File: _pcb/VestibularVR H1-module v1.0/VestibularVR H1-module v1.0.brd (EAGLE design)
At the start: 55.9 x 56.9 mm, 73 parts, among them IC1 FT232RL, IC2 74LVC1G07DBV, IC3 TLV70033DDCR, IC4 74LVC1G07DBV, IC5 74LVC1G07DBV, IC6 74LVC1G07DBV, IC7 USBLC6-2SC6, IC8 ATXMEGA32A4U, J5 Optical_flow_1, J6 Optical_flow_2, X1 TSW-105-02-S-D, X7 22-23-2051

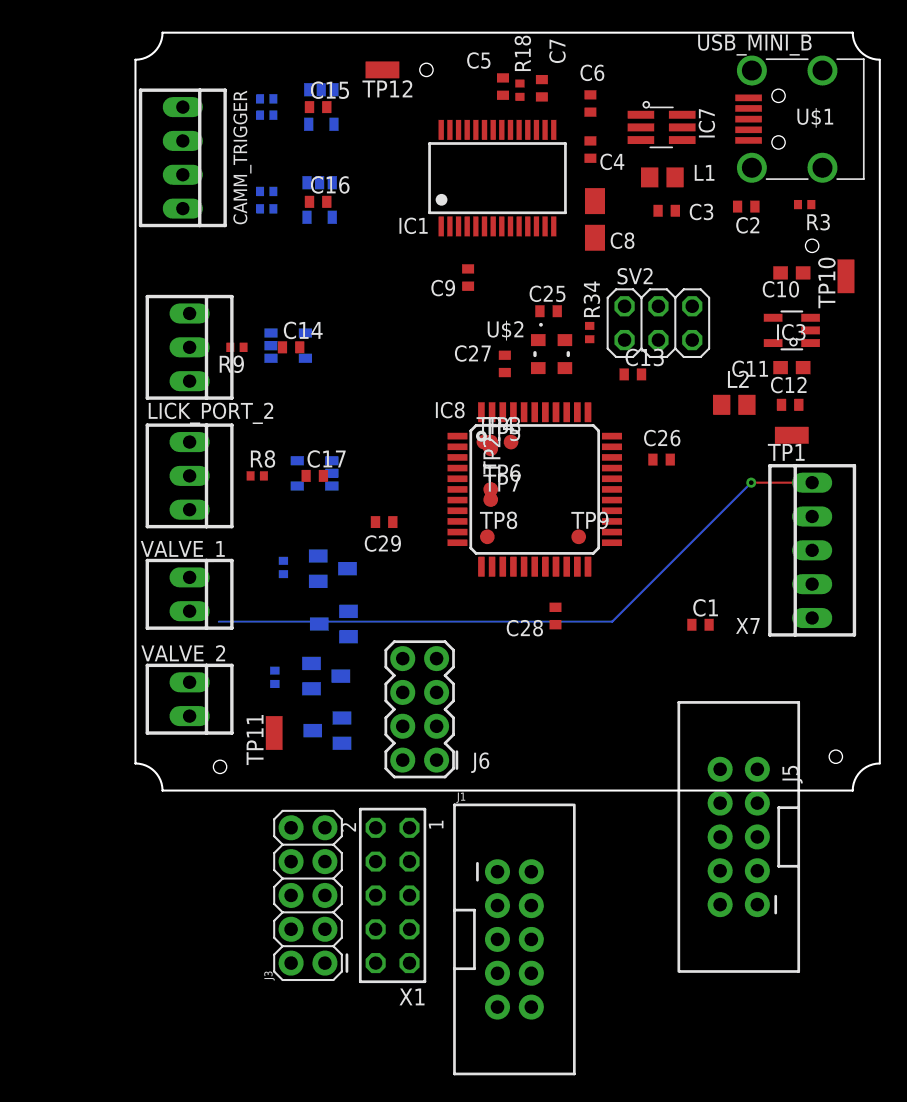
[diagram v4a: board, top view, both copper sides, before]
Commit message: . schm design reviewed 2nd time with Filipe . pcb design already started; not finished
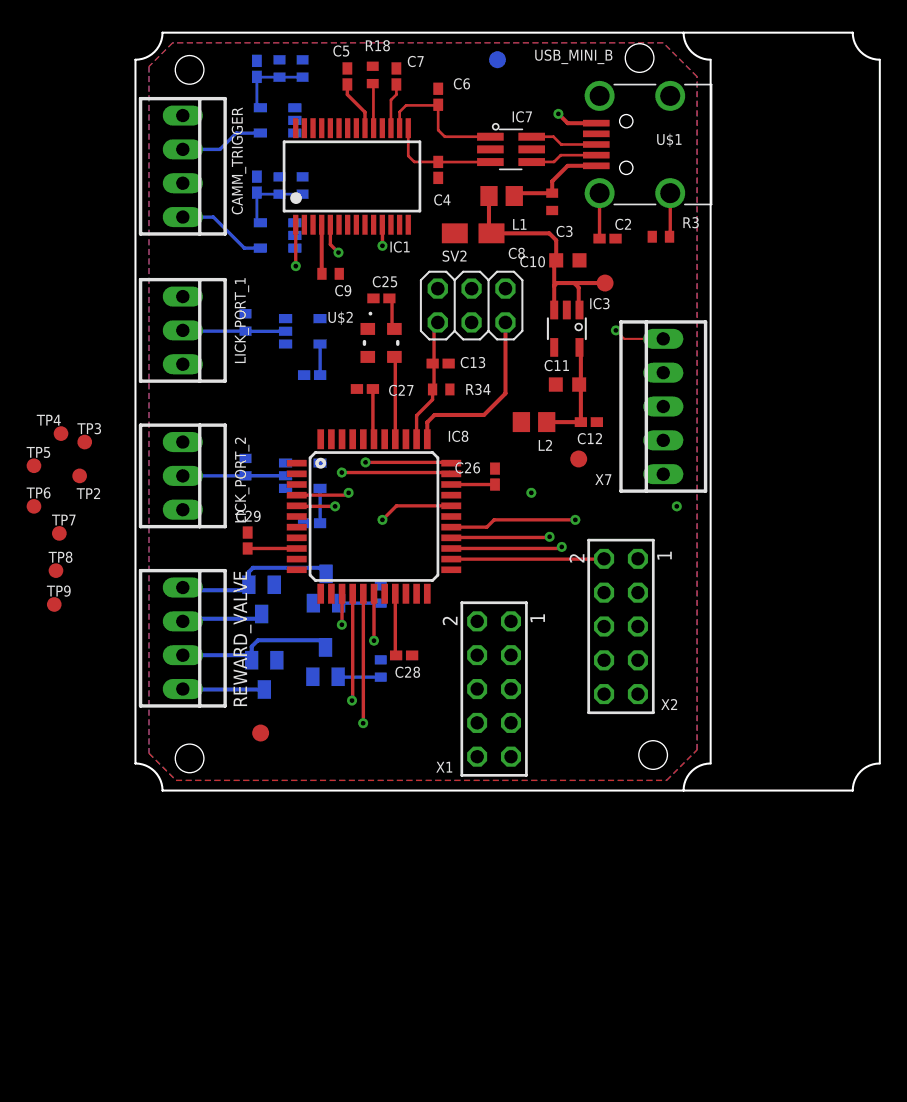
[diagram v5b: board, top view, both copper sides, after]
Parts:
- removed C1: 100nF, rcl:C0402
- removed J1: (no value), SparkFun-Connectors:2X5-SHROUDED
- removed J3: (no value), SparkFun-Connectors:2X5
- removed J5: Optical_flow_1, SparkFun-Connectors:2X5-SHROUDED_LOCK
- removed J6: Optical_flow_2, SparkFun-Connectors:2X4
- removed TP12: WIREPADSMD1,27-254, wirepad:SMD1,27-2,54
- removed VALVE_1, VALVE_2: 22-23-2021, con-molex:22-23-2021
- added REWARD_VALVE: 22-23-2041, con-molex:22-23-2041
- added TP13: TPB1,27, testpad:B1,27
- added X2: TSW-105-02-S-D, con-samtec:TSW-105-02-S-D
- C10, C11: device rcl:C0603 -> rcl:C0603K
- C12, C13, C14, C15, C16, C17, C2, C25, C26, C27, C28, C29, C4, C5, C6, C7: device rcl:C0402 -> rcl:C0402K
- TP1, TP10, TP11: value WIREPADSMD1,27-254 -> TPB1,27; device wirepad:SMD1,27-2,54 -> testpad:B1,27
- moved TP10 55.7 mm to (9.40, 4.32)
- moved TP11 53.3 mm to (27.2, 54.9), flipped to the bottom
- moved TP9 39.7 mm to (-6.10, 14.0)
- moved TP5 34.3 mm to (-7.62, 24.4)
- moved TP6 34.3 mm to (-7.62, 21.3)
- moved TP7 32.5 mm to (-5.71, 19.3)
- moved TP2 32.5 mm to (-4.19, 23.6)
- moved TP8 32.5 mm to (-5.97, 16.5)
- moved TP4 31.8 mm to (-5.59, 26.8)
- moved TP3 30.5 mm to (-3.81, 26.2)
- moved X1 17.3 mm to (26.9, 7.62)
- moved IC3 16.9 mm to (32.4, 34.7), turned to 180 degrees
- moved C11 16.9 mm to (32.4, 30.5), turned to 180 degrees
- moved C10 16.8 mm to (32.5, 39.8), turned to 0 degrees
- moved TP1 16.1 mm to (33.3, 24.9), turned to 0 degrees
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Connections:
- removed net N$9: D1.1, U$6.3, VALVE_1.1
- net +12V: now also D4.3, REWARD_VALVE.2, REWARD_VALVE.4; no longer VALVE_1.2
- net +3V3: now also TP1.TP, X1.1, X2.1; no longer J5.1, J6.1, TP1.1
- net +3V3_U: no longer C1.1
- net +5V: now also TP13.TP; no longer TP10.1
- net GND: now also TP10.TP, TP11.TP, X1.7, X2.7; no longer C1.2, J5.7, J6.7, TP11.1, TP12.1
- net N$6: now also REWARD_VALVE.3; no longer VALVE_2.1
- net N$7: now also D1.1, REWARD_VALVE.1, U$6.3; no longer D4.3, VALVE_2.2
- net U_OPTICAL_FLOW_1_CS: now also X1.2; no longer J5.2
- net U_OPTICAL_FLOW_1_INT: now also X1.5; no longer J5.5
- net U_OPTICAL_FLOW_1_MISO: now also X1.8; no longer J5.8
- net U_OPTICAL_FLOW_1_MOSI: now also X1.6; no longer J5.6
- net U_OPTICAL_FLOW_1_SCK: now also X1.4; no longer J5.4
- net U_OPTICAL_FLOW_2_CS: now also X2.2; no longer J6.2
- net U_OPTICAL_FLOW_2_INT: now also X2.5; no longer J6.5
- net U_OPTICAL_FLOW_2_MISO: now also X2.8; no longer J6.8
- net U_OPTICAL_FLOW_2_MOSI: now also X2.6; no longer J6.6
- net U_OPTICAL_FLOW_2_SCK: now also X2.4; no longer J6.4
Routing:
- net U_OPTICAL_FLOW_2_INT: track 0.00 -> 40.1 mm, vias 0 -> 2
- net U_OPTICAL_FLOW_1_INT: track 0.00 -> 33.6 mm, vias 0 -> 2
- net +12V: track 48.9 -> 16.1 mm
- net FTDI_TXD: track 0.00 -> 28.3 mm, vias 0 -> 2
- net FTDI_CTS: track 0.00 -> 27.8 mm, vias 0 -> 2
- net FTDI_RXD: track 0.00 -> 25.4 mm, vias 0 -> 2
- net +5V: track 0.00 -> 23.3 mm
- net U_OPTICAL_FLOW_2_MISO: track 0.00 -> 20.2 mm, vias 0 -> 1
- net U_OPTICAL_FLOW_1_MISO: track 0.00 -> 18.3 mm, vias 0 -> 1
- net +3V3_U: track 0.00 -> 18.0 mm
- net U_OPTICAL_FLOW_1_MOSI: track 0.00 -> 17.8 mm, vias 0 -> 1
- net +3V3: track 0.00 -> 17.0 mm
- net U_OPTICAL_FLOW_2_MOSI: track 0.00 -> 16.8 mm, vias 0 -> 1
- net U_OPTICAL_FLOW_2_SCK: track 0.00 -> 15.9 mm, vias 0 -> 1
- net PDI_DATA: track 0.00 -> 13.4 mm
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- added copper zone on layer 1, net GND
- added copper zone on layer 16, net GND
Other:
- outline, holes or cut-outs redrawn

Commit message: same as last commit: . procceding pcb design
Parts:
- moved TP10 24.7 mm to (34.0, 2.29)
- moved TP9 14.2 mm to (-5.59, 28.2)
- moved TP8 11.8 mm to (-7.24, 28.2)
- moved TP6 5.89 mm to (-8.38, 27.2)
- moved TP7 5.80 mm to (-2.92, 24.4)
- moved TP5 5.24 mm to (-2.79, 26.4)
- moved TP2 4.13 mm to (-6.99, 26.7)
- moved R1 2.81 mm to (9.76, 54.0)
- moved R5 2.45 mm to (10.1, 45.2)
- moved R6 2.05 mm to (12.8, 45.2)
- moved C10 2.04 mm to (30.4, 39.6), turned to 180 degrees
- moved R2 1.80 mm to (12.6, 54.0)
- moved TP11 1.48 mm to (25.9, 54.1)
- moved TP1 1.19 mm to (34.2, 24.1)
- moved TP13 1.05 mm to (34.2, 37.8)
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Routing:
- net +3V3: track 17.0 -> 210.1 mm, vias 0 -> 10
- net +12V: track 16.1 -> 126.7 mm, vias 1 -> 2
- net +3V3_U: track 18.0 -> 113.0 mm, vias 0 -> 8
- net +5V: track 23.3 -> 99.2 mm, vias 0 -> 7
- net U_CAM2_TRIGGER: track 0.00 -> 43.7 mm, vias 0 -> 2
- net HARP_H1_CLOCK_IN: track 0.00 -> 38.4 mm, vias 0 -> 2
- net HARP_H1_BOARD_RX: track 0.00 -> 33.1 mm, vias 0 -> 2
- net FTDI_RTS: track 0.00 -> 32.9 mm, vias 0 -> 2
- net HARP_H1_BOARD_TX: track 0.00 -> 31.2 mm, vias 0 -> 2
- net U_CAM1_TRIGGER: track 0.00 -> 29.4 mm, vias 0 -> 2
- net U_REWARD_VALVE_2: track 3.21 -> 30.6 mm, vias 0 -> 3
- net U_REWARD_VALVE_1: track 3.16 -> 21.4 mm, vias 0 -> 2
- net U_LICK_PORT_1: track 0.00 -> 11.7 mm, vias 0 -> 1
- net U_LICK_PORT_2: track 0.00 -> 8.89 mm, vias 0 -> 1
- net GND: track 3.14 -> 11.5 mm, vias 1 -> 9
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- added copper zone on layer 1, net 123
- added copper zone on layer 2, net 123
- added copper zone on layer 2, net GND
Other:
- board size 55.9 x 56.9 mm -> 43 x 56.5 mm

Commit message: . pcb design; not finnished
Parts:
- added R10: 910, rcl:R0402
- added STATE: (no value), led:CHIP-LED0603
- R1, R18, R2, R3, R34, R4, R5, R6, R7, R8, R9: device rcl:R0402 -> rcl:R0402@1
- moved R7 0.25 mm to (18.3, 8.40)
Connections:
- new net N$9: R10.2, STATE.C
- net GND: now also R10.1
- net LED_STATE: now also STATE.A
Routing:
- net LED_STATE: track 0.00 -> 33.2 mm, vias 0 -> 3
- net N$9: track 0.00 -> 2.05 mm
- net U_CAM2_TRIGGER: track 43.7 -> 45.6 mm
- net +12V: track 126.7 -> 127.5 mm
- net +3V3: track 210.1 -> 209.5 mm
- net GND: vias 9 -> 47
- added copper zone on layer 1, net +3V3
- added copper zone on layer 15, net +3V3
- added copper zone on layer 16, net +3V3
- added copper zone on layer 2, net +3V3
- added copper zone on layer 1, net +5V
- added copper zone on layer 15, net +5V
- added copper zone on layer 16, net +5V
- added copper zone on layer 2, net +5V
- added copper zone on layer 1, net 1
- added copper zone on layer 15, net GND
- added copper zone on layer 2, net N$19
- added copper zone on layer 16, net N$20
- added copper zone on layer 1, net N$21
- added copper zone on layer 15, net N$22
- added copper zone on layer 16, net N$23
- added copper zone on layer 2, net N$24
- added copper zone on layer 1, net N$25
- added copper zone on layer 15, net N$26
- added copper zone on layer 16, net N$27
- added copper zone on layer 2, net N$28
- added copper zone on layer 1, net N$29
- added copper zone on layer 15, net N$30
- added copper zone on layer 16, net N$31
- added copper zone on layer 2, net N$32
- added copper zone on layer 1, net N$33
- added copper zone on layer 15, net N$34
- added copper zone on layer 16, net N$35
- added copper zone on layer 2, net N$36
- added copper zone on layer 1, net N$37
- added copper zone on layer 15, net N$39
- added copper zone on layer 16, net N$40
- added copper zone on layer 2, net N$41
- added copper zone on layer 1, net N$42
- added copper zone on layer 15, net N$43
- added copper zone on layer 16, net N$44
- added copper zone on layer 2, net N$45
- added copper zone on layer 1, net N$46
- added copper zone on layer 15, net N$47
- added copper zone on layer 16, net N$48
- added copper zone on layer 2, net N$49
- added copper zone on layer 1, net N$50
- added copper zone on layer 15, net N$51
- added copper zone on layer 16, net N$52
- added copper zone on layer 16, net N$53
- added copper zone on layer 1, net N$54
- added copper zone on layer 2, net N$55
- added copper zone on layer 1, net N$56
- added copper zone on layer 16, net N$57
- added copper zone on layer 2, net N$58
- added copper zone on layer 1, net N$60
- added copper zone on layer 15, net N$61
- added copper zone on layer 16, net N$62
- added copper zone on layer 16, net N$63
- added copper zone on layer 16, net N$64
- added copper zone on layer 16, net N$65
- added copper zone on layer 16, net N$66
- added copper zone on layer 16, net N$67
- removed copper zone on layer 2, net 123
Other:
- board text added: "Vestibular VR H1 Module"

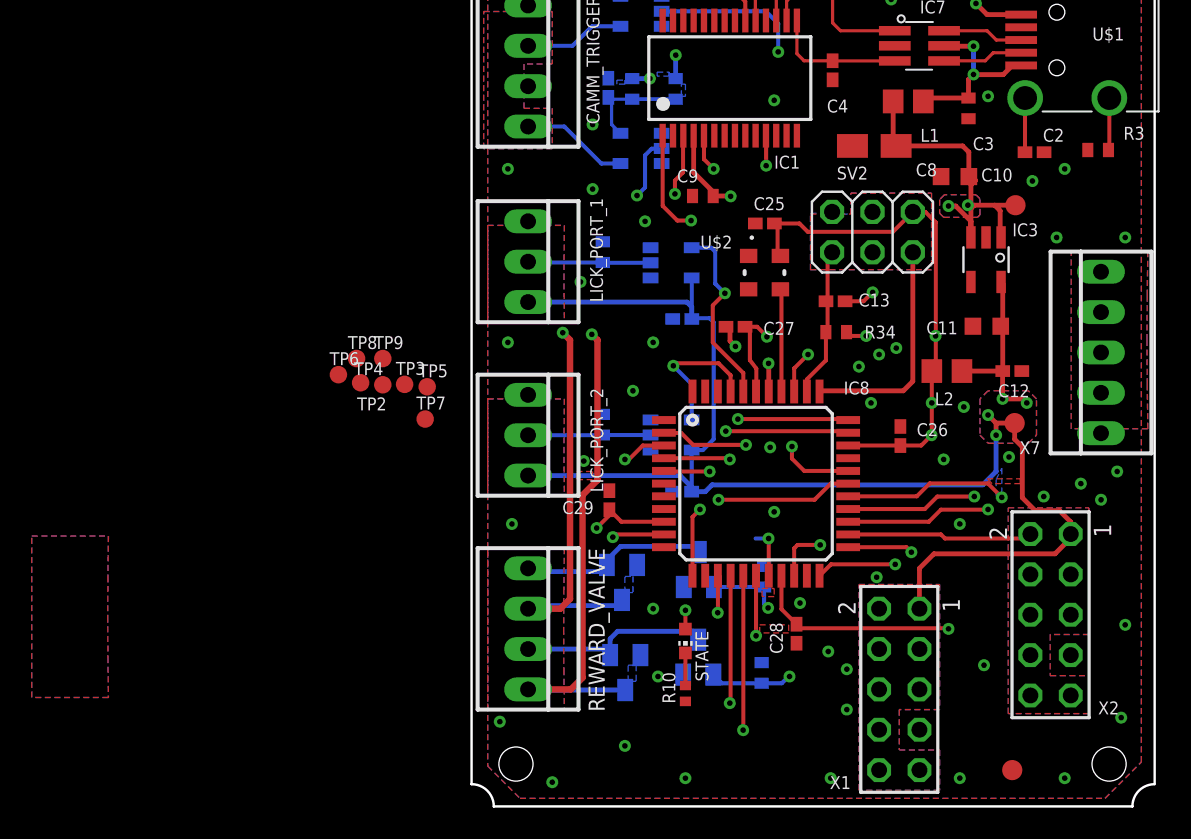
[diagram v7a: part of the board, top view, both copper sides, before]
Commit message: . 1st stage pcb design finnalized . missing:   . put couple test poitns   . move mechanical hole from one to other side usb plug . Filipe going to do a revision
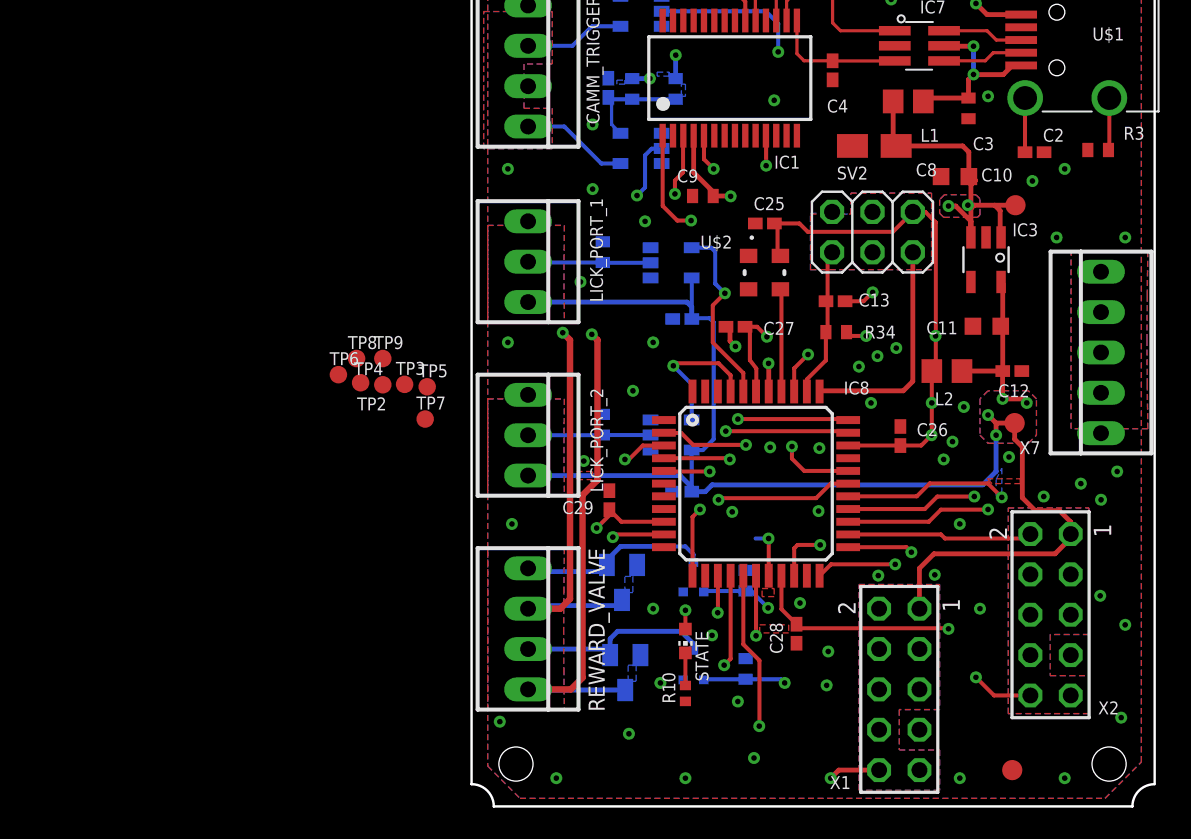
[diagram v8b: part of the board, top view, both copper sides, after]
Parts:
- removed U$5, U$6: DMN2005K, VestibularVR H1-module v1.0:SOT23
- added U$4, U$7: DMG1012UW, VestibularVR H1-module v1.0:SOT323
- moved R4 1.20 mm to (17.2, 14.2)
- moved R7 1.05 mm to (17.2, 8.65)
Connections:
- removed net N$7: D1.1, REWARD_VALVE.1, U$6.3
- new net N$68: D1.1, REWARD_VALVE.1, U$4.3
- net GND: now also U$4.2, U$7.2, X1.10, X2.10; no longer U$5.2, U$6.2
- net N$6: now also U$7.3; no longer U$5.3
- net U_OPTICAL_FLOW_1_INT: now also X1.6; no longer X1.5
- net U_OPTICAL_FLOW_1_MISO: now also X1.5; no longer X1.8
- net U_OPTICAL_FLOW_1_MOSI: now also X1.4; no longer X1.6
- net U_OPTICAL_FLOW_1_SCK: now also X1.3; no longer X1.4
- net U_OPTICAL_FLOW_2_INT: now also X2.6; no longer X2.5
- net U_OPTICAL_FLOW_2_MISO: now also X2.5; no longer X2.8
- net U_OPTICAL_FLOW_2_MOSI: now also X2.4; no longer X2.6
- net U_OPTICAL_FLOW_2_SCK: now also X2.3; no longer X2.4
- net U_REWARD_VALVE_1: now also U$4.1; no longer U$6.1
- net U_REWARD_VALVE_2: now also U$7.1; no longer U$5.1
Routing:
- net N$68: track 0.00 -> 12.1 mm
- net N$7: track 11.8 -> 0.00 mm
- net GND: track 11.5 -> 18.7 mm, vias 47 -> 55
- net U_OPTICAL_FLOW_2_INT: track 40.1 -> 43.8 mm
- net U_OPTICAL_FLOW_1_SCK: track 11.9 -> 14.7 mm
- net U_OPTICAL_FLOW_1_MISO: track 18.3 -> 21.1 mm
- net N$14: track 9.60 -> 6.87 mm
- net U_OPTICAL_FLOW_2_MOSI: track 18.1 -> 15.4 mm
- net U_OPTICAL_FLOW_2_SCK: track 16.7 -> 18.6 mm
- net U_OPTICAL_FLOW_1_MOSI: track 17.8 -> 16.0 mm
- net U_OPTICAL_FLOW_1_INT: track 35.0 -> 36.8 mm
- net LED_STATE: track 33.2 -> 34.2 mm
- net +3V3_U: track 113.0 -> 113.5 mm
- added copper zone on layer 2, net N$69
- added copper zone on layer 2, net N$7
- removed copper zone on layer 2, net N$24
- removed copper zone on layer 1, net N$25
- removed copper zone on layer 15, net N$26
- removed copper zone on layer 16, net N$27
